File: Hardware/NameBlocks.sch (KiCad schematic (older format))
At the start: 0 parts

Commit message: Add files via upload
Created ATTiny828 part in KiCad
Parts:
- added U?: ATTiny828, symbol ATTiny828
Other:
- note added: "Power should be applied with a momentary button\nthat latches a transistor circuit. Discretes or an IC?"
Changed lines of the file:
@@
 LIBS:contrib
 LIBS:valves
+LIBS:NameBlocks-cache
 EELAYER 25 0
 EELAYER END
@@
 Text Notes 7350 7500 0    60   ~ 0
 Name Display Blocks
+$Comp
+L ATTiny828 U?
+U 1 1 5A3068CA
+P 2500 1800
+F 0 "U?" H 1400 2500 60  0000 C CNN
+F 1 "ATTiny828" H 3200 2500 60  0000 C CNN
+F 2 "" H 2500 1800 60  0001 C CNN
+F 3 "" H 2500 1800 60  0001 C CNN
+	1    2500 1800
+	1    0    0    -1
+$EndComp
+Text Notes 4500 900  0    60   ~ 0
+Power should be applied with a momentary button\nthat latches a transistor circuit. Discretes or an IC?
 $EndSCHEMATC

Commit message: Created Kingbright symbol, MAX16054 symbol
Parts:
- added BT?: Battery_Cell, symbol Battery_Cell
- added J?: CONN_01X04_MALE, symbol CONN_01X04_MALE
- added J?: CONN_01X04_FEMALE, symbol CONN_01X04_FEMALE
- added Q?: Q_PMOS_DGS, symbol Q_PMOS_DGS
- added R?: 1M, symbol R_Small
- added RN? (x2): R_Pack08, symbol R_Pack08
- added TP? (x2): TEST, symbol TEST
- added U?: Alphanumeric_SMD, symbol Alphanumeric_SMD
- added U?: MAX16054, symbol MAX16054
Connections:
- net labels added: GND, PowerOFF, VCC, uC_switch
- wire segments 0 -> 51
- no-connect marks 0 -> 3
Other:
- note added: "Momentary \nPush Button"
- note removed: "Power should be applied with a momentary button\nthat latches a transistor circuit. Discretes or an IC?"
- moved on the sheet: U?

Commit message: Added 5 pin port, power switch IC
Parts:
- removed J?: CONN_01X04_MALE, symbol CONN_01X04_MALE
- removed J?: CONN_01X04_FEMALE, symbol CONN_01X04_FEMALE
- added D? (x3): D, symbol D
- added J?: MFGPN: 3020-06-0300-00, symbol CONN_02X03
- added J? (x2): CONN_01X05, symbol CONN_01X05
- added R? (x4): 1M, symbol R_Small
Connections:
- net labels added: Button, uC_power
- net labels removed: uC_switch
- wire segments 51 -> 74
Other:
- note added: "ISP header"
- note added: "Incoming lines need pulldown resistors\nto avoid a false HIGH signal"
- note added: "Outgoing signal lines need a diode"
- note added: "Pin 1 is Button Line to ensure simultaneous power-up.\nPins 2, 3, 4 are signal lines.\nPin 5 is shared common."
- moved on the sheet: RN?, TP?, U?

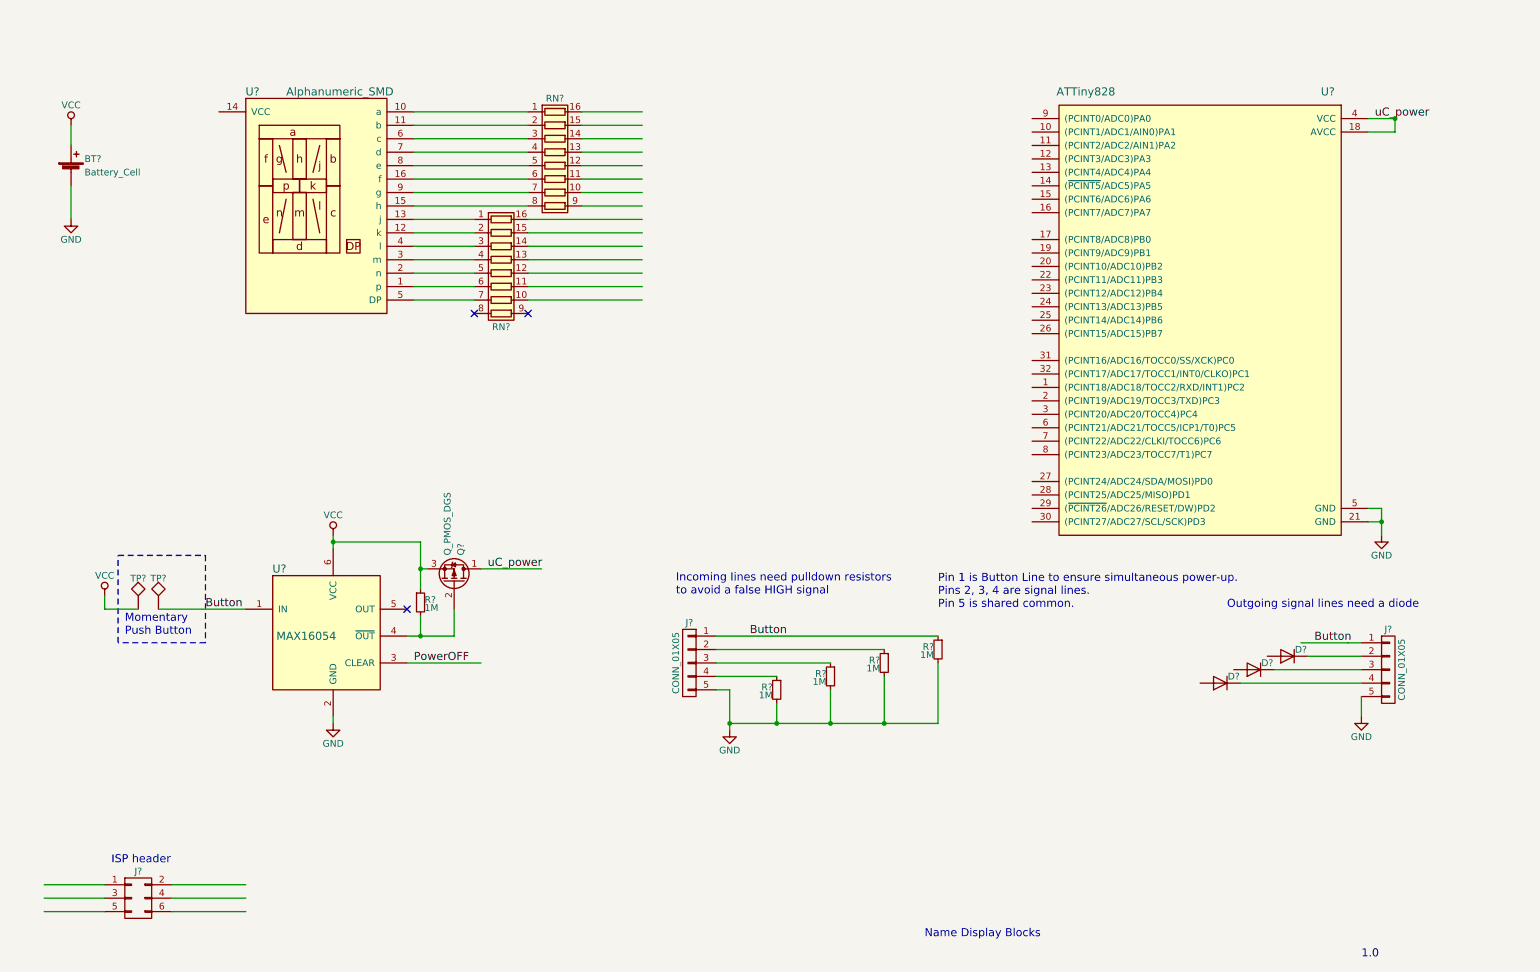
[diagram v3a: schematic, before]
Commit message: Finished schematic, all footprints and BOM chosen except switch.
StopLightTest successful. Software is now going to be on hold until I get boards in.
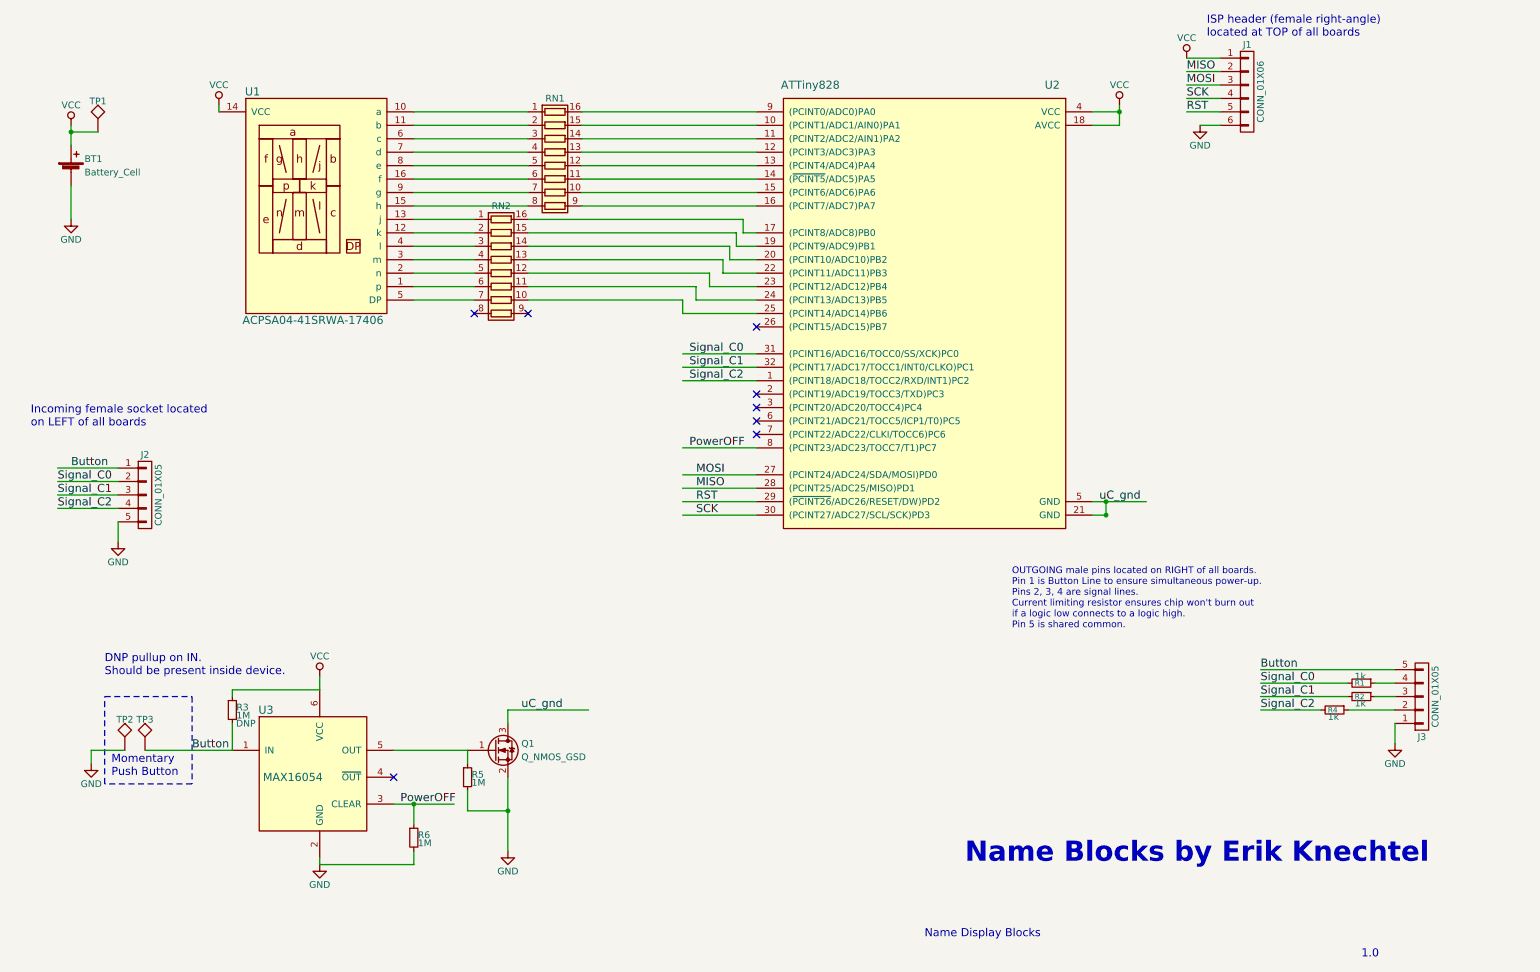
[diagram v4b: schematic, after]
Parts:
- removed D? (x3): D, symbol D
- removed J?: MFGPN: 3020-06-0300-00, symbol CONN_02X03
- removed Q?: Q_PMOS_DGS, symbol Q_PMOS_DGS
- removed R? (x4): 1M, symbol R_Small
- removed RN?: R_Pack08, symbol R_Pack08
- added J1: CONN_01X06, Socket_Strips:Socket_Strip_Angled_1x06_Pitch2.54mm, symbol CONN_01X06
- added Q1: Q_NMOS_GSD, TO_SOT_Packages_SMD:SC-59_Handsoldering, symbol Q_NMOS_GSD
- added R1, R2, R4: 1k, Resistors_SMD:R_1206_HandSoldering, symbol R_Small
- added R3, R6: 1M, Resistors_SMD:R_1206_HandSoldering, symbol R_Small
- added RN2: 180, Housings_SSOP:SSOP-16_3.9x4.9mm_Pitch0.635mm, symbol R_Pack08
- added TP1: TEST, Wire_Pads:SolderWirePad_single_1mmDrill, symbol TEST
- BT1: renamed from BT?; footprint (none) -> Battery_Holders:Keystone_1058_1x2032-CoinCell
- J2, J3: renamed from J?; footprint (none) -> Socket_Strips:Socket_Strip_Angled_1x05_Pitch2.54mm
- R5: renamed from R?; footprint (none) -> Resistors_SMD:R_1206_HandSoldering
- RN1: renamed from RN?; value R_Pack08 -> 180; footprint (none) -> Housings_SSOP:SSOP-16_3.9x4.9mm_Pitch0.635mm; MFGPN (none) -> VSSR1603181JUF
- TP2, TP3: renamed from TP?; footprint (none) -> Wire_Pads:SolderWirePad_single_1mmDrill
- U1: renamed from U?; value Alphanumeric_SMD -> ACPSA04-41SRWA-17406
- U2: renamed from U?; footprint (none) -> Housings_QFP:TQFP-32_7x7mm_Pitch0.8mm
- U3: renamed from U?; footprint (none) -> TO_SOT_Packages_SMD:SOT-23-6_Handsoldering
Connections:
- net labels added: MISO, MOSI, RST, SCK, Signal_C0, Signal_C1, Signal_C2, uC_gnd
- net labels removed: uC_power
- wire segments 74 -> 100
- no-connect marks 3 -> 8
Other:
- note added: "DNP pullup on IN.\nShould be present inside device."
- note added: "ISP header (female right-angle)\nlocated at TOP of all boards"
- note added: "Incoming female socket located \non LEFT of all boards"
- note added: "Name Blocks by Erik Knechtel"
- note added: "OUTGOING male pins located on RIGHT of all boards.\nPin 1 is Button Line to ensure simultaneous power-up.\nPins 2, 3, 4 are signal lines.\nCurrent limiting resistor ensures chip won't burn out \nif a logic low connects to a logic high.\nPin 5 is shared common."
- note removed: "ISP header"
- note removed: "Incoming lines need pulldown resistors\nto avoid a false HIGH signal"
- note removed: "Outgoing signal lines need a diode"
- note removed: "Pin 1 is Button Line to ensure simultaneous power-up.\nPins 2, 3, 4 are signal lines.\nPin 5 is shared common."
- moved on the sheet: J2, J3, R5, TP2, TP3, U2, U3

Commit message: Finished all footprints. Time for layout!
And I double checked the LED display footprint. Miraculous!
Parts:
- removed TP2, TP3: TEST, Wire_Pads:SolderWirePad_single_1mmDrill, symbol TEST
- added C1: 0.1u, Capacitors_SMD:C_1206_HandSoldering, symbol C_Small
- added S1: Button, Buttons_Switches_SMD:SW_SPST_PTS645, symbol Button
- U1: footprint (none) -> ACPSA04_Alphanumeric_LED:ACPSA04_Alphanumeric_LED
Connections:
- wire segments 100 -> 101
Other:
- note added: "Remove batteries BEFORE plugging in programmer!"
- note added: "To turn ON: Push Button\nTo turn OFF: Push Button again and \nMAX16054 will shut off OUT"
- note added: "Winter 2017-2018"
- note removed: "Momentary \nPush Button"
- moved on the sheet: Q1, R3, R5, R6, TP1, U3

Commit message: Started layout. What a mess!
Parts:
- removed R3: 1M, Resistors_SMD:R_1206_HandSoldering, symbol R_Small
- removed TP1: TEST, Wire_Pads:SolderWirePad_single_1mmDrill, symbol TEST
- BT1: footprint Battery_Holders:Keystone_1058_1x2032-CoinCell -> Battery_Holders:CR2032_SMD_BatteryHolder_BU2032SM-BT-GTR
- C1: footprint Capacitors_SMD:C_1206_HandSoldering -> Capacitors_SMD:C_0805_HandSoldering
- R1, R2, R4, R5, R6: footprint Resistors_SMD:R_1206_HandSoldering -> Resistors_SMD:R_0805_HandSoldering
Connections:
- net labels added: Signal_In_C3, Signal_In_C4, Signal_In_C5, Signal_Out_C0, Signal_Out_C1, Signal_Out_C2
- net labels removed: Signal_C0, Signal_C1, Signal_C2
- no-connect marks 8 -> 5
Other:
- note removed: "DNP pullup on IN.\nShould be present inside device."
- note removed: "Remove batteries BEFORE plugging in programmer!"
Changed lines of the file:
@@
 F 0 "BT1" H 1100 1900 50  0000 L CNN
 F 1 "Battery_Cell" H 1100 1800 50  0000 L CNN
-F 2 "Battery_Holders:Keystone_1058_1x2032-CoinCell" V 1000 1860 50  0001 C CNN
+F 2 "Battery_Holders:CR2032_SMD_BatteryHolder_BU2032SM-BT-GTR" V 1000 1860 50  0001 C CNN
 F 3 "" V 1000 1860 50  0001 C CNN
 	1    1000 1800
@@
 NoConn ~ 4000 2850
 $Comp
-L VCC #PWR4
+L VCC #PWR01
 U 1 1 5A383D97
 P 1000 1350
-F 0 "#PWR4" H 1000 1200 50  0001 C CNN
+F 0 "#PWR01" H 1000 1200 50  0001 C CNN
 F 1 "VCC" H 1000 1500 50  0000 C CNN
 F 2 "" H 1000 1350 50  0001 C CNN
@@
 $EndComp
 $Comp
-L GND #PWR7
+L GND #PWR02
 U 1 1 5A383DC9
 P 1000 2150
-F 0 "#PWR7" H 1000 1900 50  0001 C CNN
+F 0 "#PWR02" H 1000 1900 50  0001 C CNN
 F 1 "GND" H 1000 2000 50  0000 C CNN
 F 2 "" H 1000 2150 50  0001 C CNN
@@
 $EndComp
 $Comp
-L GND #PWR13
+L GND #PWR03
 U 1 1 5A3872BB
 P 3400 7250
-F 0 "#PWR13" H 3400 7000 50  0001 C CNN
+F 0 "#PWR03" H 3400 7000 50  0001 C CNN
 F 1 "GND" H 3400 7100 50  0000 C CNN
 F 2 "" H 3400 7250 50  0001 C CNN
@@
 $EndComp
 $Comp
-L VCC #PWR9
+L VCC #PWR04
 U 1 1 5A3872DE
 P 3400 5850
-F 0 "#PWR9" H 3400 5700 50  0001 C CNN
+F 0 "#PWR04" H 3400 5700 50  0001 C CNN
 F 1 "VCC" H 3400 6000 50  0000 C CNN
 F 2 "" H 3400 5850 50  0001 C CNN
@@
 Wire Wire Line
 	3400 5850 3400 5950
-Wire Wire Line
-	2100 6400 2750 6400
 Wire Wire Line
 	3400 7200 3400 7250
@@
 F 0 "R5" H 4530 6620 50  0000 L CNN
 F 1 "1M" H 4530 6560 50  0000 L CNN
-F 2 "Resistors_SMD:R_1206_HandSoldering" H 4500 6600 50  0001 C CNN
+F 2 "Resistors_SMD:R_0805_HandSoldering" H 4500 6600 50  0001 C CNN
 F 3 "" H 4500 6600 50  0001 C CNN
 	1    4500 6600
@@
 $EndComp
 $Comp
-L GND #PWR10
+L GND #PWR05
 U 1 1 5A3AFE18
 P 10850 6050
-F 0 "#PWR10" H 10850 5800 50  0001 C CNN
+F 0 "#PWR05" H 10850 5800 50  0001 C CNN
 F 1 "GND" H 10850 5900 50  0000 C CNN
 F 2 "" H 10850 6050 50  0001 C CNN
@@
 OUTGOING male pins located on RIGHT of all boards.\nPin 1 is Button Line to ensure simultaneous power-up.\nPins 2, 3, 4 are signal lines.\nCurrent limiting resistor ensures chip won't burn out \nif a logic low connects to a logic high.\nPin 5 is shared common.
 Wire Wire Line
-	10300 5800 9850 5800
-Wire Wire Line
-	9850 5700 10500 5700
-Wire Wire Line
-	10500 5600 9850 5600
+	9600 5800 10300 5800
+Wire Wire Line
+	9600 5700 10500 5700
+Wire Wire Line
+	9600 5600 10500 5600
 Text Label 2350 6400 0    60   ~ 0
 Button
@@
 Button
 $Comp
-L GND #PWR8
+L GND #PWR06
 U 1 1 5A3B1FDC
 P 1350 4550
-F 0 "#PWR8" H 1350 4300 50  0001 C CNN
+F 0 "#PWR06" H 1350 4300 50  0001 C CNN
 F 1 "GND" H 1350 4400 50  0000 C CNN
 F 2 "" H 1350 4550 50  0001 C CNN
@@
 	1350 4400 1350 4550
 Wire Wire Line
-	900  4000 1350 4000
-Text Label 1000 4000 0    60   ~ 0
+	750  4000 1350 4000
+Text Label 800  4000 0    60   ~ 0
 Button
 Wire Wire Line
-	900  4100 1350 4100
+	750  4100 1350 4100
 Wire Wire Line
 	8700 4350 8600 4350
@@
 uC_gnd
 $Comp
-L GND #PWR11
+L GND #PWR07
 U 1 1 5A5BF1E1
 P 1200 6800
-F 0 "#PWR11" H 1200 6550 50  0001 C CNN
+F 0 "#PWR07" H 1200 6550 50  0001 C CNN
 F 1 "GND" H 1200 6650 50  0000 C CNN
 F 2 "" H 1200 6800 50  0001 C CNN
@@
 	4800 6100 5400 6100
 $Comp
-L GND #PWR12
+L GND #PWR08
 U 1 1 5A5C11DF
 P 4800 7150
-F 0 "#PWR12" H 4800 6900 50  0001 C CNN
+F 0 "#PWR08" H 4800 6900 50  0001 C CNN
 F 1 "GND" H 4800 7000 50  0000 C CNN
 F 2 "" H 4800 7150 50  0001 C CNN
@@
 	4500 6400 4500 6500
 $Comp
-L VCC #PWR3
+L VCC #PWR09
 U 1 1 5A5C1DBD
 P 8800 1300
-F 0 "#PWR3" H 8800 1150 50  0001 C CNN
+F 0 "#PWR09" H 8800 1150 50  0001 C CNN
 F 1 "VCC" H 8800 1450 50  0000 C CNN
 F 2 "" H 8800 1300 50  0001 C CNN
@@
 Connection ~ 8700 4250
 $Comp
-L VCC #PWR2
+L VCC #PWR010
 U 1 1 5A5C3432
 P 2100 1300
-F 0 "#PWR2" H 2100 1150 50  0001 C CNN
+F 0 "#PWR010" H 2100 1150 50  0001 C CNN
 F 1 "VCC" H 2100 1450 50  0000 C CNN
 F 2 "" H 2100 1300 50  0001 C CNN
@@
 	9850 5500 10850 5500
 Wire Wire Line
-	6100 3150 5550 3150
-Wire Wire Line
-	6100 3250 5550 3250
-Wire Wire Line
-	6100 3350 5550 3350
-Text Label 5600 3150 0    60   ~ 0
-Signal_C0
-Text Label 5600 3250 0    60   ~ 0
-Signal_C1
-Text Label 5600 3350 0    60   ~ 0
-Signal_C2
-Text Label 9850 5600 0    60   ~ 0
-Signal_C0
-Text Label 9850 5700 0    60   ~ 0
-Signal_C1
-Text Label 9850 5800 0    60   ~ 0
-Signal_C2
-Wire Wire Line
-	1350 4200 900  4200
-Wire Wire Line
-	1350 4300 900  4300
-Text Label 900  4100 0    60   ~ 0
-Signal_C0
-Text Label 900  4200 0    60   ~ 0
-Signal_C1
-Text Label 900  4300 0    60   ~ 0
-Signal_C2
+	5350 3150 6100 3150
+Wire Wire Line
+	5350 3250 6100 3250
+Wire Wire Line
+	5350 3350 6100 3350
+Text Label 5400 3150 0    60   ~ 0
+Signal_Out_C0
+Text Label 5400 3250 0    60   ~ 0
+Signal_Out_C1
+Text Label 5400 3350 0    60   ~ 0
+Signal_Out_C2
+Wire Wire Line
+	750  4200 1350 4200
+Wire Wire Line
+	750  4300 1350 4300
+Text Label 800  4100 0    60   ~ 0
+Signal_In_C3
+Text Label 800  4200 0    60   ~ 0
+Signal_In_C4
+Text Label 800  4300 0    60   ~ 0
+Signal_In_C5
 Wire Wire Line
 	6100 4050 5550 4050
@@
 F 0 "R6" H 4130 7070 50  0000 L CNN
 F 1 "1M" H 4130 7010 50  0000 L CNN
-F 2 "Resistors_SMD:R_1206_HandSoldering" H 4100 7050 50  0001 C CNN
+F 2 "Resistors_SMD:R_0805_HandSoldering" H 4100 7050 50  0001 C CNN
 F 3 "" H 4100 7050 50  0001 C CNN
 	1    4100 7050
 	1    0    0    -1
 $EndComp
-$Comp
-L R_Small R3
-U 1 1 5A5EF3C2
-P 2750 6100
-F 0 "R3" H 2780 6120 50  0000 L CNN
-F 1 "1M" H 2780 6060 50  0000 L CNN
-F 2 "Resistors_SMD:R_1206_HandSoldering" H 2750 6100 50  0001 C CNN
-F 3 "" H 2750 6100 50  0001 C CNN
-F 4 "DNP" H 2850 6000 50  0000 C CNN "DNP"
-	1    2750 6100
-	1    0    0    -1
-$EndComp
-Wire Wire Line
-	2750 6000 2750 5950
-Wire Wire Line
-	2750 5950 3400 5950
-Wire Wire Line
-	2750 6400 2750 6200
-Text Notes 1650 5850 0    60   ~ 0
-DNP pullup on IN.\nShould be present inside device.
 Wire Wire Line
 	4100 6950 4100 6800
@@
 RST
 $Comp
-L TEST TP1
-U 1 1 5A5F18B9
-P 1200 1400
-F 0 "TP1" H 1200 1600 50  0000 C BNN
-F 1 "TEST" H 1200 1650 50  0001 C CNN
-F 2 "Wire_Pads:SolderWirePad_single_1mmDrill" H 1200 1400 50  0001 C CNN
-F 3 "" H 1200 1400 50  0001 C CNN
-	1    1200 1400
-	1    0    0    -1
-$EndComp
-Wire Wire Line
-	1200 1400 1000 1400
-Connection ~ 1000 1400
-$Comp
 L CONN_01X06 J1
 U 1 1 5A5F2F1E
@@
 ISP header (female right-angle)\nlocated at TOP of all boards
 $Comp
-L GND #PWR5
+L GND #PWR011
 U 1 1 5A5F3604
 P 9400 1450
-F 0 "#PWR5" H 9400 1200 50  0001 C CNN
+F 0 "#PWR011" H 9400 1200 50  0001 C CNN
 F 1 "GND" H 9400 1300 50  0000 C CNN
 F 2 "" H 9400 1450 50  0001 C CNN
@@
 	9550 1450 9400 1450
 $Comp
-L VCC #PWR1
+L VCC #PWR012
 U 1 1 5A5F3BEC
 P 9300 950
-F 0 "#PWR1" H 9300 800 50  0001 C CNN
+F 0 "#PWR012" H 9300 800 50  0001 C CNN
 F 1 "VCC" H 9300 1100 50  0000 C CNN
 F 2 "" H 9300 950 50  0001 C CNN
@@
 $EndComp
 NoConn ~ 6100 2950
-NoConn ~ 6100 3450
-NoConn ~ 6100 3550
-NoConn ~ 6100 3650
 NoConn ~ 6100 3750
 $Comp
@@
 F 0 "R1" V 10600 5550 40  0000 L CNN
 F 1 "1k" V 10550 5550 50  0000 L CNN
-F 2 "Resistors_SMD:R_1206_HandSoldering" H 10600 5600 50  0001 C CNN
+F 2 "Resistors_SMD:R_0805_HandSoldering" H 10600 5600 50  0001 C CNN
 F 3 "" H 10600 5600 50  0001 C CNN
 	1    10600 5600
@@
 F 0 "R2" V 10600 5650 40  0000 L CNN
 F 1 "1k" V 10650 5650 50  0000 L CNN
-F 2 "Resistors_SMD:R_1206_HandSoldering" H 10600 5700 50  0001 C CNN
+F 2 "Resistors_SMD:R_0805_HandSoldering" H 10600 5700 50  0001 C CNN
 F 3 "" H 10600 5700 50  0001 C CNN
 	1    10600 5700
@@
 F 0 "R4" V 10400 5750 40  0000 L CNN
 F 1 "1k" V 10450 5750 50  0000 L CNN
-F 2 "Resistors_SMD:R_1206_HandSoldering" H 10400 5800 50  0001 C CNN
+F 2 "Resistors_SMD:R_0805_HandSoldering" H 10400 5800 50  0001 C CNN
 F 3 "" H 10400 5800 50  0001 C CNN
 	1    10400 5800
@@
 F 0 "C1" H 8810 1820 50  0000 L CNN
 F 1 "0.1u" H 8810 1670 50  0000 L CNN
-F 2 "Capacitors_SMD:C_1206_HandSoldering" H 8800 1750 50  0001 C CNN
+F 2 "Capacitors_SMD:C_0805_HandSoldering" H 8800 1750 50  0001 C CNN
 F 3 "" H 8800 1750 50  0001 C CNN
 	1    8800 1750
@@
 Connection ~ 8800 1450
 $Comp
-L GND #PWR6
+L GND #PWR013
 U 1 1 5A65046A
 P 8800 2000
-F 0 "#PWR6" H 8800 1750 50  0001 C CNN
+F 0 "#PWR013" H 8800 1750 50  0001 C CNN
 F 1 "GND" H 8800 1850 50  0000 C CNN
 F 2 "" H 8800 2000 50  0001 C CNN
@@
 Wire Wire Line
 	1000 1350 1000 1600
-Text Notes 550  950  0    60   ~ 0
-Remove batteries BEFORE plugging in programmer!
 Text Notes 8150 7650 0    60   ~ 0
 Winter 2017-2018
@@
 Connection ~ 1200 6600
 Wire Wire Line
-	2100 6600 2100 6400
+	2100 6400 2750 6400
+Wire Wire Line
+	2100 6600 2150 6600
+Wire Wire Line
+	2150 6600 2150 6400
+Connection ~ 2150 6400
+Wire Wire Line
+	5350 3450 6100 3450
+Wire Wire Line
+	5350 3550 6100 3550
+Wire Wire Line
+	5350 3650 6100 3650
+Text Label 5400 3450 0    60   ~ 0
+Signal_In_C3
+Text Label 5400 3550 0    60   ~ 0
+Signal_In_C4
+Text Label 5400 3650 0    60   ~ 0
+Signal_In_C5
+Text Label 9650 5600 0    60   ~ 0
+Signal_Out_C0
+Text Label 9650 5700 0    60   ~ 0
+Signal_Out_C1
+Text Label 9650 5800 0    60   ~ 0
+Signal_Out_C2
 $EndSCHEMATC

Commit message: Added note in layout to update TSSOP footprints
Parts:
- BT1: MFGPN (none) -> BU2032SM-BT-GTR
- Q1: value Q_NMOS_GSD -> N-MOSFET
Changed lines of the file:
@@
 F 2 "Battery_Holders:CR2032_SMD_BatteryHolder_BU2032SM-BT-GTR" V 1000 1860 50  0001 C CNN
 F 3 "" V 1000 1860 50  0001 C CNN
+F 4 "BU2032SM-BT-GTR" H 1000 1800 60  0001 C CNN "MFGPN"
 	1    1000 1800
 	1    0    0    -1
@@
 P 4600 1750
 F 0 "RN1" V 4100 1750 50  0000 C CNN
-F 1 "180" V 5000 1750 50  0001 C CNN
+F 1 "180" V 5050 1750 50  0000 C CNN
 F 2 "Housings_SSOP:SSOP-16_3.9x4.9mm_Pitch0.635mm" V 5075 1750 50  0001 C CNN
 F 3 "" H 4600 1750 50  0001 C CNN
@@
 P 4200 2550
 F 0 "RN2" V 3700 2550 50  0000 C CNN
-F 1 "180" V 4600 2550 50  0001 C CNN
+F 1 "180" V 4600 2550 50  0000 C CNN
 F 2 "Housings_SSOP:SSOP-16_3.9x4.9mm_Pitch0.635mm" V 4675 2550 50  0001 C CNN
 F 3 "" H 4200 2550 50  0001 C CNN
@@
 U 1 1 5A6037F5
 P 4700 6400
-F 0 "Q1" H 4900 6450 50  0000 L CNN
-F 1 "Q_NMOS_GSD" H 4900 6350 50  0000 L CNN
+F 0 "Q1" H 4900 6500 50  0000 L CNN
+F 1 "N-MOSFET" H 4900 6400 50  0000 L CNN
 F 2 "TO_SOT_Packages_SMD:SC-59_Handsoldering" H 4900 6500 50  0001 C CNN
-F 3 "" H 4700 6400 50  0001 C CNN
+F 3 "DMN1019USN-13DICT-ND" H 4900 6300 50  0000 L CNN
 	1    4700 6400
 	1    0    0    -1
